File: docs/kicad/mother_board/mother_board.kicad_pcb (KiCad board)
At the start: 2 copper layers, 70 x 50 mm, 15 parts, among them J1 EXPR, J2 TFT_CONTROL, J3 TFT_DATA, J4 SERIAL, J5 LEDS, J6 ROTARY12, J7 ROTARY34, J8 SW_OUT, J9 SW_IN, U1 myTeensy3.6

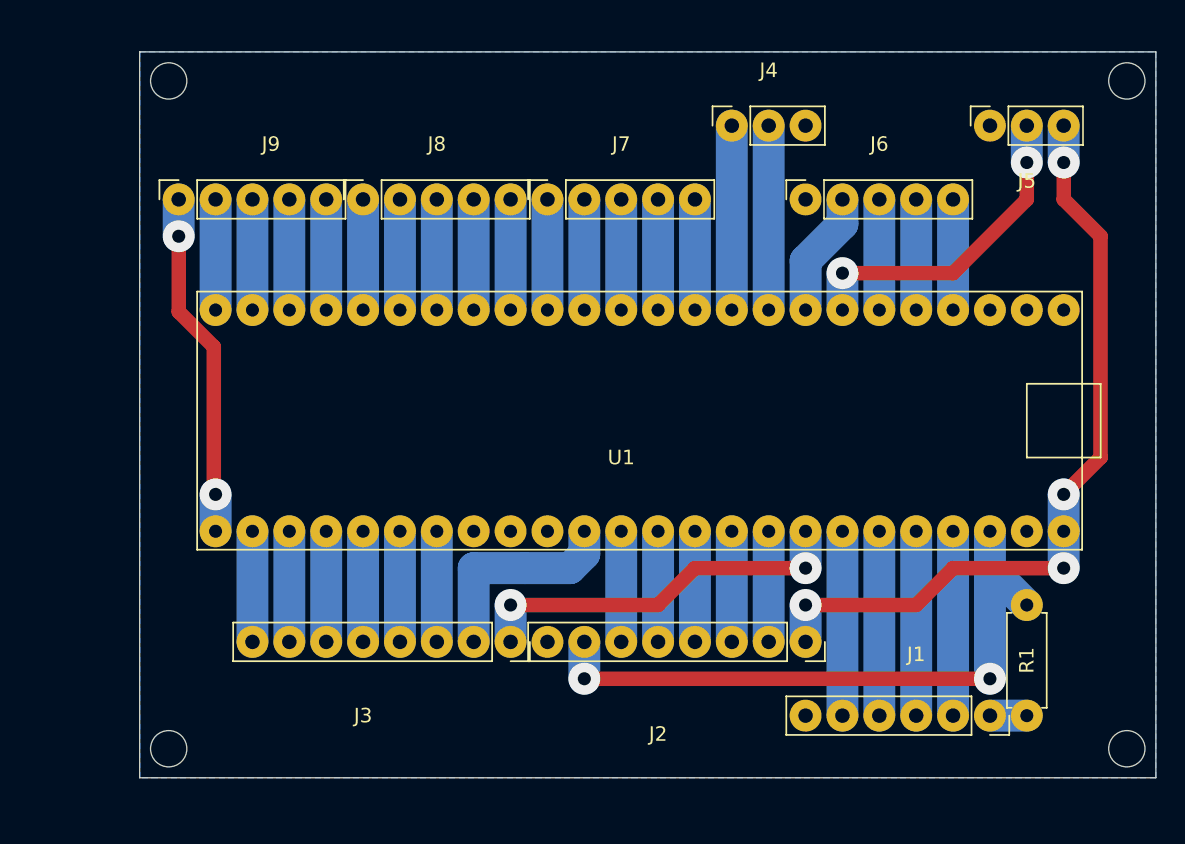
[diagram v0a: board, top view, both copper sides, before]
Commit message: docs/kicad - added new display_connector, reworked tentative new PCB
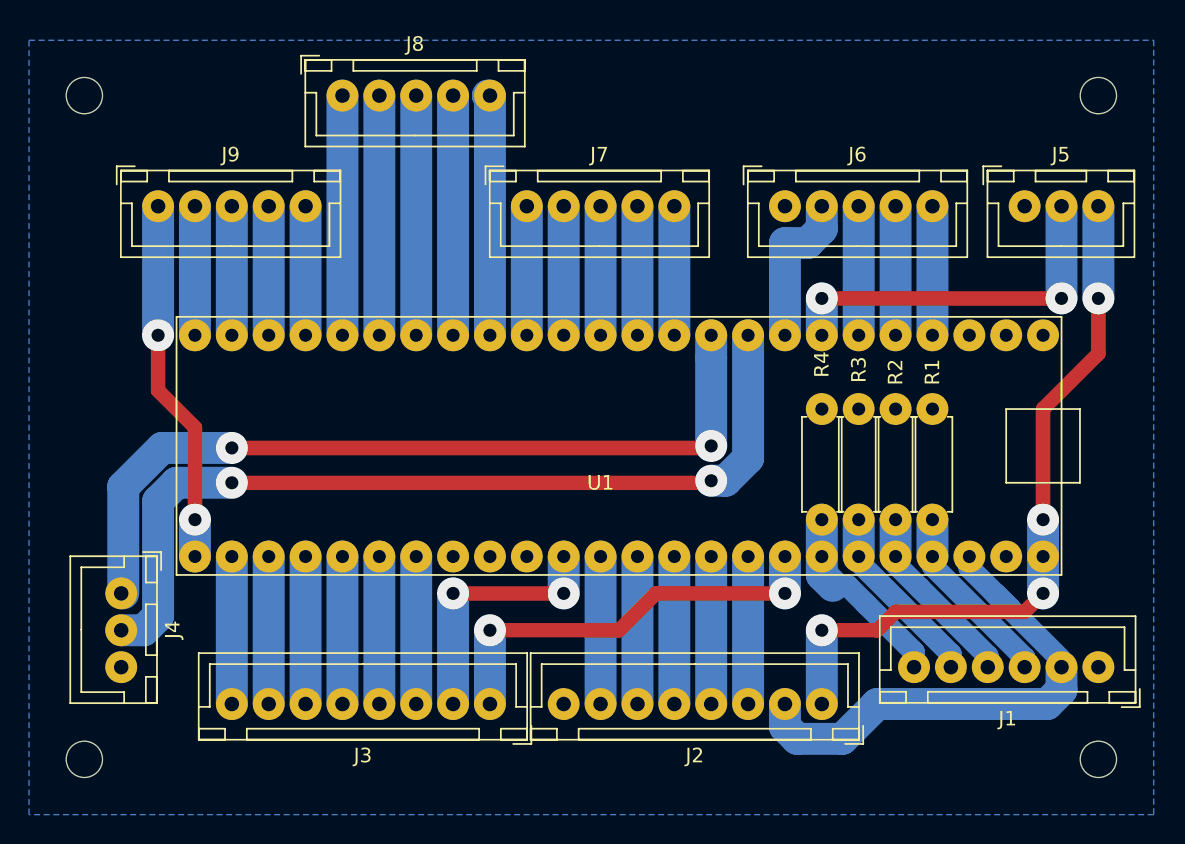
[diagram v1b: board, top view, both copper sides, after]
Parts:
- removed the REF** at (2.00, -48.0)
- removed the REF** at (2.00, -2.00)
- removed the REF** at (68.0, -2.00)
- added R2: 10K, 0_my_footprints:myResistor, F.Cu at (52.1, -17.8)
- added R3: 10K, 0_my_footprints:myResistor, F.Cu at (49.5, -17.8)
- added R4: 10K, 0_my_footprints:myResistor, F.Cu at (47.0, -17.8)
- added REF**: myMountingHole_2.5mm, 0_my_footprints:myMountingHole_2.5mm, F.Cu at (-3.81, -47.0)
- added REF**: myMountingHole_2.5mm, 0_my_footprints:myMountingHole_2.5mm, F.Cu at (66.0, -1.27)
- added REF**: myMountingHole_2.5mm, 0_my_footprints:myMountingHole_2.5mm, F.Cu at (66.0, -47.0)
- J1: footprint 0_my_footprints:myPinSocket_1x06 -> 0_my_footprints:myJSTx06
- J2, J3: footprint 0_my_footprints:myPinSocket_1x08 -> 0_my_footprints:myJSTx08
- J4, J5: footprint 0_my_footprints:myPinSocket_1x03 -> 0_my_footprints:myJSTx03
- J6, J7, J8, J9: footprint 0_my_footprints:myPinSocket_1x05 -> 0_my_footprints:myJSTx05
- R1: value 1K -> 10K
- moved REF** 85.7 mm to (-3.81, -1.27)
- moved J4 53.0 mm to (-1.27, -12.7), turned to 270 degrees
- moved R1 15.0 mm to (54.6, -17.8)
- moved J1 8.18 mm to (66.0, -7.62), turned to 180 degrees
- moved J8 7.29 mm to (14.0, -47.0), turned to 0 degrees
- moved J5 6.04 mm to (61.0, -39.4), turned to 0 degrees
- moved J3 4.51 mm to (24.1, -5.08), turned to 180 degrees
- moved J2 4.42 mm to (47.0, -5.08), turned to 180 degrees
- moved U1 2.25 mm to (33.0, -22.9)
- moved J9 1.50 mm to (1.27, -39.4), turned to 0 degrees
- moved J7 1.50 mm to (26.7, -39.4), turned to 0 degrees
- moved J6 1.50 mm to (44.5, -39.4), turned to 0 degrees
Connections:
- J1 pad 1: Net-(J1-Pad1) -> GND
- J1 pad 2: EXPR1 -> +3V3
- J1 pad 3: EXPR2 -> EXPR1
- J1 pad 4: EXPR3 -> EXPR2
- J1 pad 5: EXPR4 -> EXPR3
- J1 pad 6: GND -> EXPR4
- J2 pad 2: TFT_RES -> +3V3
- J2 pad 3: TFT_CS -> TFT_RES
- J2 pad 4: TFT_CD_RS -> TFT_CS
- J2 pad 5: TFT_WR -> TFT_CD_RS
- J2 pad 6: TFT_RD -> TFT_WR
- J2 pad 7: +3V3 -> TFT_RD
- R1 pad 1: Net-(J1-Pad1) -> EXPR1
- R1 pad 2: +3V3 -> GND
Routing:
- net RX3: track 12.7 -> 61.2 mm, vias 0 -> 2
- net TX3: track 12.7 -> 56.6 mm, vias 0 -> 2
- net SW_OUT1: track 7.62 -> 16.7 mm
- net SW_OUT5: track 7.62 -> 16.5 mm
- net SW_OUT4: track 7.62 -> 16.5 mm
- net SW_OUT3: track 7.62 -> 16.5 mm
- net SW_OUT2: track 7.62 -> 16.5 mm
- net +3V3: track 51.9 -> 44.0 mm, vias 2 -> 0
- net +5V: track 54.0 -> 49.6 mm
- net TFT_DAT0: track 14.7 -> 17.8 mm, vias 0 -> 2
- net LEDS: track 22.4 -> 25.4 mm
- net TFT_DAT1: track 26.5 -> 29.0 mm
- net TFT_WR: track 7.62 -> 10.2 mm
- net TFT_RES: track 7.62 -> 10.2 mm
- net TFT_RD: track 7.62 -> 10.2 mm
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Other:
- board outline removed

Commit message: start MAKE NEW motherboard and display_connector FOR olds TeensyExprssion box with TE2 code
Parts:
- removed the REF** at (-3.81, -47.0)
- removed the REF** at (66.0, -1.27)
- removed the REF** at (66.0, -47.0)
- added REF**: myMountingHole_2.5mm, 0_my_footprints:myMountingHole_2.5mm, F.Cu at (2.00, -48.0)
- added REF**: myMountingHole_2.5mm, 0_my_footprints:myMountingHole_2.5mm, F.Cu at (68.0, -2.00)
- added REF**: myMountingHole_2.5mm, 0_my_footprints:myMountingHole_2.5mm, F.Cu at (68.0, -48.0)
- J1: footprint 0_my_footprints:myJSTx06 -> 0_my_footprints:myPinSocket_1x06
- J4, J5: footprint 0_my_footprints:myJSTx03 -> 0_my_footprints:myPinSocket_1x03
- J6, J7, J8, J9: footprint 0_my_footprints:myJSTx05 -> 0_my_footprints:myPinSocket_1x05
- moved J4 55.0 mm to (53.3, -6.35), turned to 90 degrees
- moved J2 20.9 mm to (26.7, -10.2), turned to 0 degrees
- moved J3 20.9 mm to (3.81, -10.2), turned to 0 degrees
- moved J1 13.3 mm to (53.3, -11.4), turned to 90 degrees
- moved J8 12.5 mm to (25.4, -41.9), turned to 270 degrees
- moved J6 11.7 mm to (55.9, -41.9), turned to 270 degrees
- moved J7 11.7 mm to (38.1, -41.9), turned to 270 degrees
- moved J9 11.7 mm to (12.7, -41.9), turned to 270 degrees
- moved REF** 5.86 mm to (2.00, -2.00)
- moved U1 4.02 mm to (34.3, -26.7)
- moved R1 4.02 mm to (55.9, -21.6)
- moved R2 4.02 mm to (53.3, -21.6)
- moved R3 4.02 mm to (50.8, -21.6)
- moved R4 4.02 mm to (48.3, -21.6)
- moved J5 2.84 mm to (62.2, -41.9), turned to 90 degrees
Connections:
- J1 pad 1: GND -> EXPR4
- J1 pad 2: +3V3 -> EXPR3
- J1 pad 3: EXPR1 -> EXPR2
- J1 pad 4: EXPR2 -> EXPR1
- J1 pad 5: EXPR3 -> +3V3
- J1 pad 6: EXPR4 -> GND
- J2 pad 1: +5V -> GND
- J2 pad 2: +3V3 -> TFT_RD
- J2 pad 3: TFT_RES -> TFT_WR
- J2 pad 4: TFT_CS -> TFT_CD_RS
- J2 pad 5: TFT_CD_RS -> TFT_CS
- J2 pad 6: TFT_WR -> TFT_RES
- J2 pad 7: TFT_RD -> +3V3
- J2 pad 8: GND -> +5V
- J3 pad 1: TFT_DAT1 -> TFT_DAT2
- J3 pad 2: TFT_DAT0 -> TFT_DAT3
- J3 pad 3: TFT_DAT7 -> TFT_DAT4
- J3 pad 4: TFT_DAT6 -> TFT_DAT5
- J3 pad 5: TFT_DAT5 -> TFT_DAT6
- J3 pad 6: TFT_DAT4 -> TFT_DAT7
- J3 pad 7: TFT_DAT3 -> TFT_DAT0
- J3 pad 8: TFT_DAT2 -> TFT_DAT1
- J6 pad 1: GND -> ROT1A
- J6 pad 2: ROT2A -> ROT1B
- J6 pad 3: ROT2B -> ROT2A
- J6 pad 4: ROT1B -> ROT2B
- J6 pad 5: ROT1A -> GND
- J7 pad 1: +3V3 -> ROT3A
- J7 pad 2: ROT4A -> ROT3B
- J7 pad 3: ROT4B -> ROT4A
- J7 pad 4: ROT3B -> ROT4B
- J7 pad 5: ROT3A -> +3V3
- J8 pad 1: SW_OUT5 -> SW_OUT0
- J8 pad 2: SW_OUT4 -> SW_OUT1
- J8 pad 3: SW_OUT3 -> SW_OUT2
- J8 pad 4: SW_OUT2 -> SW_OUT3
- J8 pad 5: SW_OUT1 -> SW_OUT4
- J9 pad 1: SW_IN5 -> SW_IN0
- J9 pad 2: SW_IN4 -> SW_IN1
- J9 pad 3: SW_IN3 -> SW_IN2
- J9 pad 4: SW_IN2 -> SW_IN3
- J9 pad 5: SW_IN1 -> SW_IN4
- U1 pad 13: ROT4B -> ROT4A
- U1 pad 14: ROT4A -> ROT4B
- U1 pad 16: SW_OUT1 -> SW_OUT0
- U1 pad 17: SW_OUT2 -> SW_OUT1
- U1 pad 18: SW_OUT3 -> SW_OUT2
- U1 pad 19: SW_OUT4 -> SW_OUT3
- U1 pad 20: SW_OUT5 -> SW_OUT4
- U1 pad 21: SW_IN1 -> SW_IN0
- U1 pad 22: SW_IN2 -> SW_IN1
- U1 pad 23: SW_IN3 -> SW_IN2
- U1 pad 24: SW_IN4 -> SW_IN3
- U1 pad 25: SW_IN5 -> SW_IN4
- U1 pad 6: ROT2B -> ROT2A
- U1 pad 8: ROT2A -> ROT2B
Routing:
- net RX3: track 61.2 -> 9.68 mm
- net TX3: track 56.6 -> 7.27 mm
- net SW_IN5: track 25.2 -> 0.00 mm, vias 2 -> 0
- net SW_OUT5: track 16.5 -> 0.00 mm
- net SW_IN4: track 8.89 -> 23.9 mm, vias 0 -> 2
- net SW_OUT1: track 16.7 -> 7.62 mm
- net SW_OUT4: track 16.5 -> 7.62 mm
- net SW_OUT3: track 16.5 -> 7.62 mm
- net SW_OUT2: track 16.5 -> 7.62 mm
- net SW_OUT0: track 0.00 -> 7.62 mm
- net SW_IN0: track 0.00 -> 7.62 mm
- net +3V3: track 44.0 -> 51.6 mm, vias 0 -> 2
- net +5V: track 49.6 -> 55.8 mm
- net TFT_RES: track 10.2 -> 15.3 mm
- net TFT_DAT3: track 10.2 -> 15.0 mm
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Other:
- board outline added: 70 x 50 mm

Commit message: kicad - corrected TFT data pin order for new teensyExpression2 board/code
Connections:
- J3 pad 1: TFT_DAT2 -> TFT_DAT0
- J3 pad 2: TFT_DAT3 -> TFT_DAT1
- J3 pad 3: TFT_DAT4 -> TFT_DAT2
- J3 pad 4: TFT_DAT5 -> TFT_DAT3
- J3 pad 5: TFT_DAT6 -> TFT_DAT4
- J3 pad 6: TFT_DAT7 -> TFT_DAT5
- J3 pad 7: TFT_DAT0 -> TFT_DAT6
- J3 pad 8: TFT_DAT1 -> TFT_DAT7
- U1 pad 26: TFT_DAT2 -> TFT_DAT0
- U1 pad 27: TFT_DAT3 -> TFT_DAT1
- U1 pad 28: TFT_DAT4 -> TFT_DAT2
- U1 pad 29: TFT_DAT5 -> TFT_DAT3
- U1 pad 30: TFT_DAT6 -> TFT_DAT4
- U1 pad 31: TFT_DAT7 -> TFT_DAT5
- U1 pad 35: TFT_DAT0 -> TFT_DAT6
- U1 pad 41: TFT_DAT1 -> TFT_DAT7
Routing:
- net TFT_DAT7: track 14.8 -> 30.8 mm, vias 0 -> 2
- net TFT_DAT1: track 30.8 -> 15.0 mm, vias 2 -> 0
- net TFT_DAT6: track 10.9 -> 22.6 mm, vias 0 -> 2
- net TFT_DAT0: track 22.6 -> 11.6 mm, vias 2 -> 0
- net TFT_DAT4: track 15.0 -> 10.9 mm
- net TFT_DAT2: track 11.6 -> 15.0 mm

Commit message: AFTER BUILD NEW PCBs - corrected display connector pins; removed old combined plot and gcode file
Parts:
- R1, R2, R3, R4: value 10K -> 47K

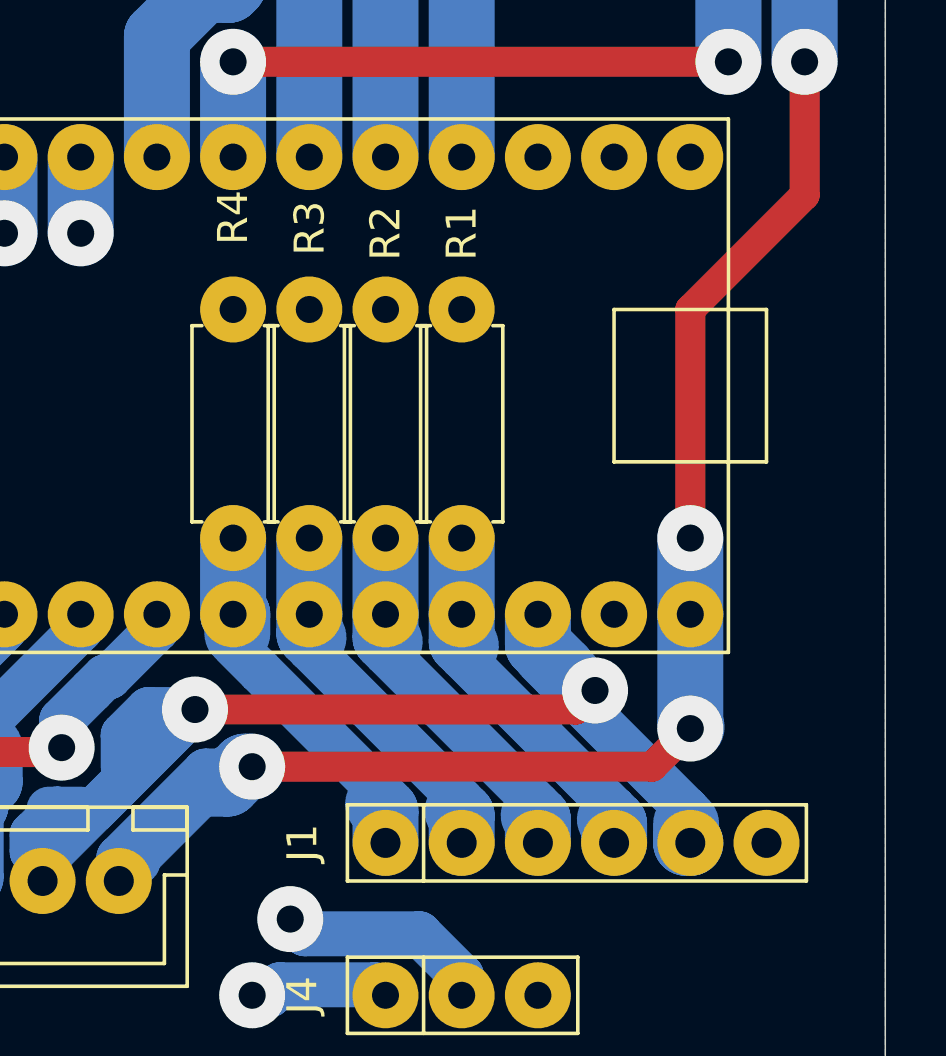
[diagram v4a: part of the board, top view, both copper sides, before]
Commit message: added 1K resistor to pedal power to keep from crashing while inserting plugs
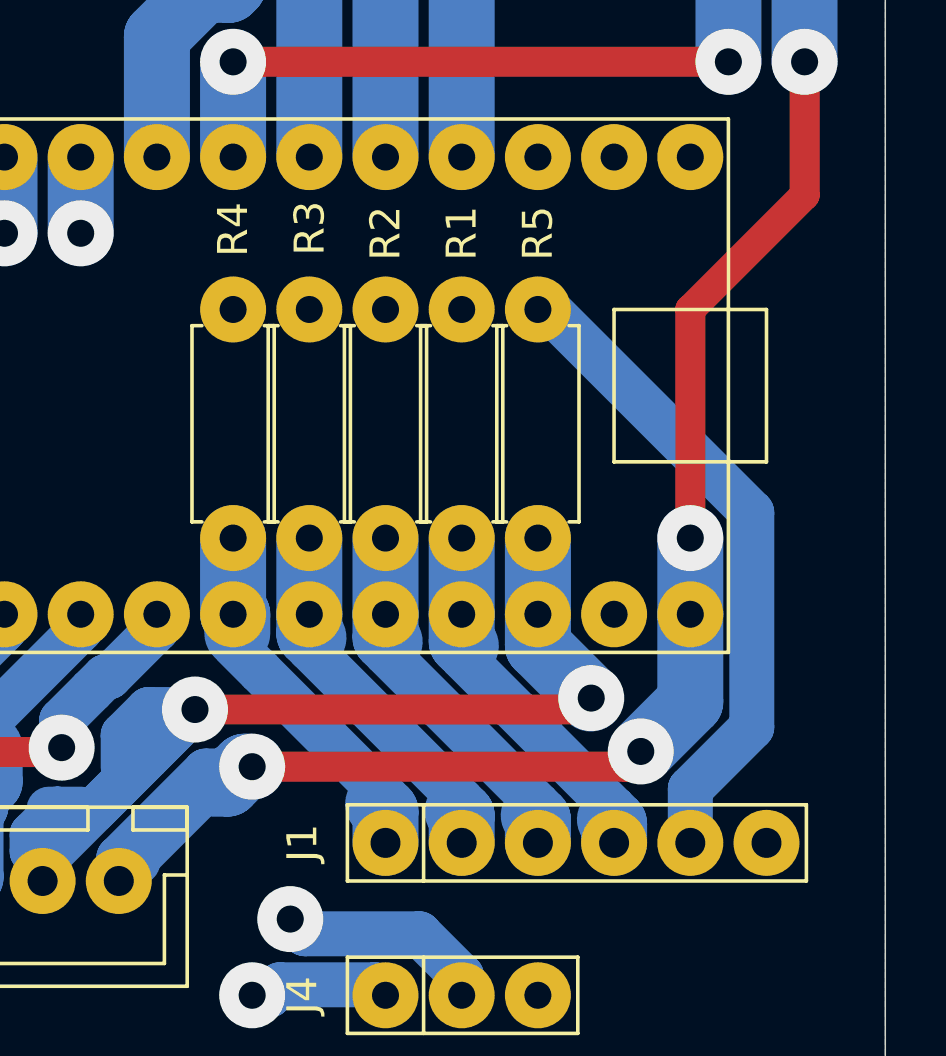
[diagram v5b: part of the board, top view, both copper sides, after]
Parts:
- added R5: 1K, 0_my_footprints:myResistor, F.Cu at (58.4, -29.2)
- R1, R2, R3, R4: value 47K -> 10K
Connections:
- J1 pad 5: +3V3 -> Net-(J1-Pad5)
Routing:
- net Net-(J1-Pad5): track 0.00 -> 21.8 mm
- net +3V3: track 51.6 -> 46.7 mm
- net +5V: track 55.8 -> 55.3 mm

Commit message: notes regarding resistors for pedals
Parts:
- R5: value 1K -> 100
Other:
- board text added: "Note that in the current board, the 100 ohm resistor is in the cable to the foot pedal sockets, and not on the board which has been modified with a wire."
